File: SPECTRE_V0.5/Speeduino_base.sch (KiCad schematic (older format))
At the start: 213 parts, among them J2 Conn_02x04_Odd_Even, J3 Conn_01x06_Male, Q1 2N7002, Q10 BSP78, Q11 BSP78, Q12 BSP78, Q13 BSP78, Q14 BSP78, Q15 BSP78, Q16 SMD-MOSFET-N-CH-55V-2.1A-AO34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, Q17 AO3401A, Q18 BSP78, Q19 SMD-MOSFET-N-CH-55V-2.1A-AO34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, Q2 CJ2302, Q20 AO3401A, Q21 SMD-MOSFET-N-CH-55V-2.1A-AO34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, Q22 SMD-MOSFET-N-CH-55V-2.1A-AO34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, Q23 AO3401A, Q24 AO3401A, Q25 BSP78, Q26 BSP78, Q3 CJ2302, Q4 CJ2302, Q5 BSP78, Q6 BSP78, Q7 CJ2302, Q8 CJ2302, Q9 CJ2302, U1 MAX9926UAEE+, U2 molex_48pin, U3 LM78M05_TO220, U4 MAX3232, U5 TL431DBZ

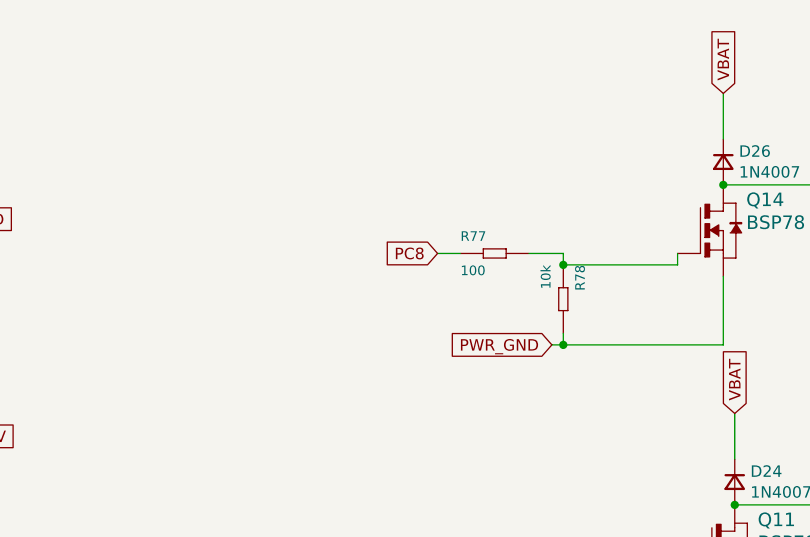
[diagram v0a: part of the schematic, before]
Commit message: boost pin change
update pin def boost pin
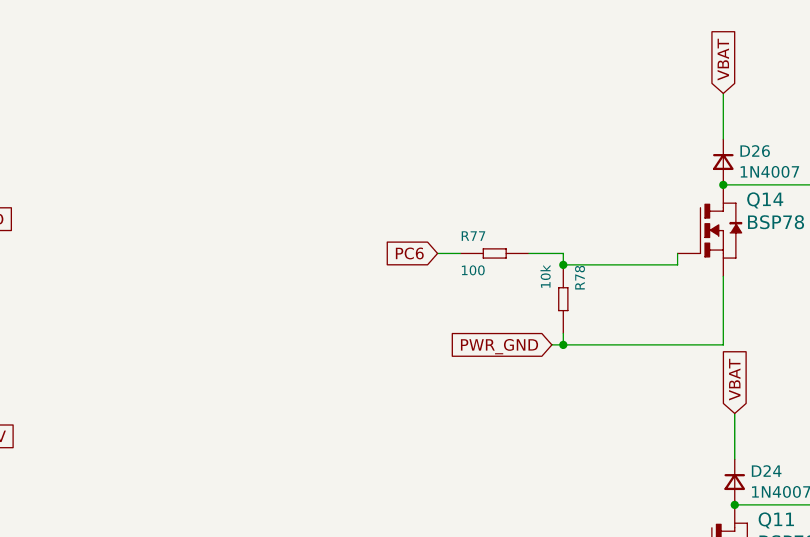
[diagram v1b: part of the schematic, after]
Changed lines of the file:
@@
 PE1
 Text GLabel 14650 1050 0    50   Input ~ 0
-PC8
+PC6
 Text GLabel 14450 3950 0    50   Input ~ 0
 PD3

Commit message: Cleaned and updated the SPECTRE V0.5 Created separate Peak and Hold board.
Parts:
- removed D10: 40V-1A, Speeduino_base:DO-214AC, symbol Speeduino_base-eagle-import:SMD-DIODE-SCHOTTKY-40V-1A(DO-214AC)
- removed D13: Zener 5.1V, Speeduino_base:LED-1206, symbol Speeduino_base-eagle-import:SMD-DIODE-SWITCHING-75V-150MA(D1206)
- added D4: 1N4007, Diode_SMD:D_SMA, symbol Device:D_Small
- added D8: Zener 5.1V, Diode_SMD:D_MiniMELF_Handsoldering, symbol Device:D_Zener_Small
- C27, C28, C29, C30: footprint Capacitor_SMD:C_0603_1608Metric -> Speeduino_base:C0603
- D14: renamed from D22; footprint Speeduino_base:D_SOD-128 -> Diode_SMD:D_SMA
- D20: renamed from D23; footprint Speeduino_base:D_SOD-128 -> Diode_SMD:D_SMA
- D27: renamed from D30; value SS310 -> 1N4007
- D28: renamed from D31; value SS310 -> 1N4007
- D29: renamed from D26; footprint Speeduino_base:D_SOD-128 -> Diode_SMD:D_SMA
- D30: renamed from D24; footprint Speeduino_base:D_SOD-128 -> Diode_SMD:D_SMA
- D31: renamed from D25; footprint Speeduino_base:D_SOD-128 -> Diode_SMD:D_SMA
- D32, D33: value SS310 -> 1N4007
- D6: renamed from D27; value 3.6V -> Zener 3.6V
- Q1: renamed from Q2; value CJ2302 -> AO3400
- Q16: renamed from Q21; value SMD-MOSFET-N-CH-55V-2.1A-AO3422(SOT-23) -> AO3422
- Q17: renamed from Q22; value SMD-MOSFET-N-CH-55V-2.1A-AO3422(SOT-23) -> AO3422
- Q2: renamed from Q1; value 2N7002 -> AO3400
- Q3: renamed from Q4; value CJ2302 -> AO3400
- Q4: renamed from Q7; value CJ2302 -> AO3400
- Q5: renamed from Q9; value CJ2302 -> AO3400
- Q6: renamed from Q8; value CJ2302 -> AO3400
- Q7: renamed from Q3; value CJ2302 -> AO3400
- Q8: renamed from Q19; value SMD-MOSFET-N-CH-55V-2.1A-AO3422(SOT-23) -> AO3422
- Q9: renamed from Q16; value SMD-MOSFET-N-CH-55V-2.1A-AO3422(SOT-23) -> AO3422
- R16: renamed from R76; footprint Resistor_SMD:R_0603_1608Metric_Pad1.05x0.95mm_HandSolder -> Speeduino_base:R0603
- R20: renamed from R72; footprint Resistor_SMD:R_0603_1608Metric_Pad1.05x0.95mm_HandSolder -> Speeduino_base:R0603
- R3: renamed from R2; footprint Resistor_SMD:R_0603_1608Metric_Pad1.05x0.95mm_HandSolder -> Speeduino_base:R0603
- R30: renamed from R98; footprint Resistor_SMD:R_0603_1608Metric_Pad1.05x0.95mm_HandSolder -> Speeduino_base:R0603
- R31: renamed from R99; footprint Resistor_SMD:R_0603_1608Metric_Pad1.05x0.95mm_HandSolder -> Speeduino_base:R0603
- R5: renamed from R75; footprint Resistor_SMD:R_0603_1608Metric_Pad1.05x0.95mm_HandSolder -> Speeduino_base:R0603
- R69: renamed from R84; value 1K -> 1k
- R73: renamed from R85; value 1K -> 1k; footprint Speeduino_base:R_0603_1608Metric_Pad1.05x0.95mm_HandSolder -> Speeduino_base:R0603
- R74: renamed from R80; value 1K -> 1k; footprint Speeduino_base:R_0603_1608Metric_Pad1.05x0.95mm_HandSolder -> Speeduino_base:R0603
- R76: renamed from R87; value 1K8 -> 1k8; footprint Speeduino_base:R_0603_1608Metric_Pad1.05x0.95mm_HandSolder -> Speeduino_base:R0603
- R77: renamed from R82; value 1K8 -> 1k8; footprint Speeduino_base:R_0603_1608Metric_Pad1.05x0.95mm_HandSolder -> Speeduino_base:R0603
- R78: renamed from R86; footprint Speeduino_base:R_0603_1608Metric_Pad1.05x0.95mm_HandSolder -> Speeduino_base:R0603
- R79: renamed from R81; footprint Speeduino_base:R_0603_1608Metric_Pad1.05x0.95mm_HandSolder -> Speeduino_base:R0603
- R80: renamed from R79; footprint Speeduino_base:R_0603_1608Metric_Pad1.05x0.95mm_HandSolder -> Speeduino_base:R0603
- R81: renamed from R88; footprint Speeduino_base:R_0603_1608Metric_Pad1.05x0.95mm_HandSolder -> Speeduino_base:R0603
- R86: renamed from R89; value 1K -> 1k; footprint Speeduino_base:R_0603_1608Metric_Pad1.05x0.95mm_HandSolder -> Speeduino_base:R0603
- R87: renamed from R90; value 1K -> 1k; footprint Speeduino_base:R_0603_1608Metric_Pad1.05x0.95mm_HandSolder -> Speeduino_base:R0603
- R91: renamed from R92; value 1K8 -> 1k8; footprint Speeduino_base:R_0603_1608Metric_Pad1.05x0.95mm_HandSolder -> Speeduino_base:R0603
- R92: renamed from R94; value 1K8 -> 1k8; footprint Speeduino_base:R_0603_1608Metric_Pad1.05x0.95mm_HandSolder -> Speeduino_base:R0603
- R96: renamed from R93; footprint Speeduino_base:R_0603_1608Metric_Pad1.05x0.95mm_HandSolder -> Speeduino_base:R0603
- R97: renamed from R91; footprint Speeduino_base:R_0603_1608Metric_Pad1.05x0.95mm_HandSolder -> Speeduino_base:R0603
- R98: renamed from R95; footprint Speeduino_base:R_0603_1608Metric_Pad1.05x0.95mm_HandSolder -> Speeduino_base:R0603
- R99: renamed from R96; footprint Speeduino_base:R_0603_1608Metric_Pad1.05x0.95mm_HandSolder -> Speeduino_base:R0603
- renumbered C7 to C10, C19 to C11, C8 to C12, C9 to C13, C18 to C14, C10 to C15, C22 to C16, C25 to C17, C26 to C18, C11 to C19, C12 to C20, C13 to C21, C15 to C22, C21 to C23, C20 to C24, C24 to C25, C23 to C26, C14 to C6, C6 to C7, C16 to C8, C17 to C9, D5 to D10, D7 to D11, D8 to D12, D9 to D13, D18 to D15, D11 to D16, D12 to D17, D17 to D18, D15 to D19, D16 to D21, D28 to D22, D29 to D23, D19 to D24, D20 to D25, D21 to D26, D4 to D5, D14 to D7, D6 to D9, J3 to J1, JP13 to JP1, JP16 to JP10, JP17 to JP11, JP3 to JP12, JP5 to JP13, JP11 to JP2, JP12 to JP3, JP14 to JP4, JP10 to JP5, JP9 to JP6, JP2 to JP7, JP4 to JP8, JP1 to JP9, Q20 to Q10, Q17 to Q11, Q15 to Q12, Q18 to Q13, Q5 to Q14, Q6 to Q15, Q10 to Q18, Q14 to Q19, Q11 to Q20, Q23 to Q21, Q24 to Q22, Q12 to Q23, Q13 to Q24, R8 to R10, R6 to R11, R9 to R12, R10 to R13, R11 to R14, R12 to R15, R13 to R17, R74 to R18, R14 to R19, R23 to R2, R16 to R21, R15 to R22, R35 to R23, R17 to R24, R36 to R25, R37 to R26, R18 to R27, R19 to R28, R20 to R29, R21 to R32, R26 to R33, R27 to R34, R22 to R35, R29 to R36, R40 to R37, R24 to R38, R25 to R39, R3 to R4, R41 to R40, R42 to R41, R66 to R42, R28 to R43, R30 to R44, R31 to R45, R67 to R46, R68 to R47, R45 to R48, R32 to R49, R33 to R50, R47 to R51, R50 to R52, R51 to R53, R34 to R56, R56 to R57, R52 to R58, R39 to R59, R5 to R6, R38 to R60, R53 to R61, R57 to R62, R43 to R63, R60 to R64, R44 to R66, R46 to R67, R83 to R68, R4 to R7, R69 to R70, R70 to R71, R71 to R72, R97 to R75, R73 to R8, R48 to R82, R49 to R83, R58 to R84, R77 to R85, R59 to R88, R61 to R89, R7 to R9, R78 to R90, R62 to R93, R63 to R94, R64 to R95, U$2 to U$1, U3 to U2, U5 to U3, U2 to U4, U?1 to U5, U4 to U6
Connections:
- wire segments 569 -> 570
- no-connect marks 52 -> 51
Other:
- moved on the sheet: D6, R31, U3

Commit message: Removed peak&hold driver from this repo. Update resistor values in schematic to values that work. Cleaned up resistor naming.
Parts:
- C27, C28, C29, C30: value 100nF -> 100nf
- R10, R26, R29, R47: value 9.1k -> 9k1
- R25: value 4.7k -> 4K7
- R28, R46, R9: value 4.7k -> 4k7
- R34, R41, R52, R55, R61, R65, R84, R85, R88: value 100 -> 100R
- R44: value 8k3 -> 33k
- R45: value 1k2 -> 5k1
- R66: value 100k -> 10k
- R67: value 1k -> 100R
- R70: value 180 -> 220R
- R71: value 82 -> 100R
- R72: value 560 -> 470R
- R75: value 120 -> 120R
- R78, R79, R96, R97: value 470 -> 470R
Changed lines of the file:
@@
 P 5900 8200
 F 0 "R45" H 5750 8250 42  0000 L BNN
-F 1 "1k2" H 5750 8100 42  0000 L BNN
+F 1 "5k1" H 5750 8100 42  0000 L BNN
 F 2 "Speeduino_base:R0603" H 5900 8200 50  0001 C CNN
 F 3 "" H 5900 8200 50  0001 C CNN
@@
 P 9650 10000
 F 0 "R65" H 9500 10050 42  0000 L BNN
-F 1 "100" H 9500 9900 42  0000 L BNN
+F 1 "100R" H 9500 9900 42  0000 L BNN
 F 2 "Speeduino_base:R0603" H 9650 10000 50  0001 C CNN
 F 3 "" H 9650 10000 50  0001 C CNN
@@
 P 14700 3950
 F 0 "R84" H 14550 4000 42  0000 L BNN
-F 1 "100" H 14550 3850 42  0000 L BNN
+F 1 "100R" H 14550 3850 42  0000 L BNN
 F 2 "Speeduino_base:R0603" H 14700 3950 50  0001 C CNN
 F 3 "" H 14700 3950 50  0001 C CNN
@@
 P 7650 3200
 F 0 "R55" H 7500 3250 42  0000 L BNN
-F 1 "100" H 7500 3100 42  0000 L BNN
+F 1 "100R" H 7500 3100 42  0000 L BNN
 F 2 "Speeduino_base:R0603" H 7650 3200 50  0001 C CNN
 F 3 "" H 7650 3200 50  0001 C CNN
@@
 P 4350 3700
 F 0 "R34" H 4200 3750 42  0000 L BNN
-F 1 "100" H 4200 3600 42  0000 L BNN
+F 1 "100R" H 4200 3600 42  0000 L BNN
 F 2 "Speeduino_base:R0603" H 4350 3700 50  0001 C CNN
 F 3 "" H 4350 3700 50  0001 C CNN
@@
 P 8350 10000
 F 0 "R61" H 8200 10050 42  0000 L BNN
-F 1 "100" H 8200 9900 42  0000 L BNN
+F 1 "100R" H 8200 9900 42  0000 L BNN
 F 2 "Speeduino_base:R0603" H 8350 10000 50  0001 C CNN
 F 3 "" H 8350 10000 50  0001 C CNN
@@
 P 6950 10000
 F 0 "R52" H 6800 10050 42  0000 L BNN
-F 1 "100" H 6800 9900 42  0000 L BNN
+F 1 "100R" H 6800 9900 42  0000 L BNN
 F 2 "Speeduino_base:R0603" H 6950 10000 50  0001 C CNN
 F 3 "" H 6950 10000 50  0001 C CNN
@@
 P 5450 10000
 F 0 "R41" H 5300 10050 42  0000 L BNN
-F 1 "100" H 5300 9900 42  0000 L BNN
+F 1 "100R" H 5300 9900 42  0000 L BNN
 F 2 "Speeduino_base:R0603" H 5450 10000 50  0001 C CNN
 F 3 "" H 5450 10000 50  0001 C CNN
@@
 P 14950 2450
 F 0 "R88" H 14800 2500 42  0000 L BNN
-F 1 "100" H 14800 2350 42  0000 L BNN
+F 1 "100R" H 14800 2350 42  0000 L BNN
 F 2 "Speeduino_base:R0603" H 14950 2450 50  0001 C CNN
 F 3 "" H 14950 2450 50  0001 C CNN
@@
 P 10050 7950
 F 0 "R67" H 9900 8000 42  0000 L BNN
-F 1 "1k" H 9900 7850 42  0000 L BNN
+F 1 "100R" H 9900 7850 42  0000 L BNN
 F 2 "Speeduino_base:R0603" H 10050 7950 50  0001 C CNN
 F 3 "" H 10050 7950 50  0001 C CNN
@@
 P 9750 8150
 F 0 "R66" H 9600 8200 42  0000 L BNN
-F 1 "100k" H 9600 8050 42  0000 L BNN
+F 1 "10k" H 9600 8050 42  0000 L BNN
 F 2 "Speeduino_base:R0603" H 9750 8150 50  0001 C CNN
 F 3 "" H 9750 8150 50  0001 C CNN
@@
 P 3150 8950
 F 0 "R25" H 3000 9009 59  0000 L BNN
-F 1 "4.7k" H 3000 8820 59  0000 L BNN
+F 1 "4K7" H 3000 8820 59  0000 L BNN
 F 2 "Speeduino_base:R0603" H 3150 8950 50  0001 C CNN
 F 3 "" H 3150 8950 50  0001 C CNN
@@
 P 3150 9550
 F 0 "R26" H 3000 9609 59  0000 L BNN
-F 1 "9.1k" H 3000 9420 59  0000 L BNN
+F 1 "9k1" H 3000 9420 59  0000 L BNN
 F 2 "Speeduino_base:R0603" H 3150 9550 50  0001 C CNN
 F 3 "" H 3150 9550 50  0001 C CNN
@@
 P 3300 7150
 F 0 "R28" H 3150 7209 59  0000 L BNN
-F 1 "4.7k" H 3150 7020 59  0000 L BNN
+F 1 "4k7" H 3150 7020 59  0000 L BNN
 F 2 "Speeduino_base:R0603" H 3300 7150 50  0001 C CNN
 F 3 "" H 3300 7150 50  0001 C CNN
@@
 P 3300 7750
 F 0 "R29" H 3150 7809 59  0000 L BNN
-F 1 "9.1k" H 3150 7620 59  0000 L BNN
+F 1 "9k1" H 3150 7620 59  0000 L BNN
 F 2 "Speeduino_base:R0603" H 3300 7750 50  0001 C CNN
 F 3 "" H 3300 7750 50  0001 C CNN
@@
 P 1350 7100
 F 0 "R9" H 1200 7159 59  0000 L BNN
-F 1 "4.7k" H 1200 6970 59  0000 L BNN
+F 1 "4k7" H 1200 6970 59  0000 L BNN
 F 2 "Speeduino_base:R0603" H 1350 7100 50  0001 C CNN
 F 3 "" H 1350 7100 50  0001 C CNN
@@
 P 1350 7700
 F 0 "R10" H 1200 7759 59  0000 L BNN
-F 1 "9.1k" H 1200 7570 59  0000 L BNN
+F 1 "9k1" H 1200 7570 59  0000 L BNN
 F 2 "Speeduino_base:R0603" H 1350 7700 50  0001 C CNN
 F 3 "" H 1350 7700 50  0001 C CNN
@@
 P 5950 4650
 F 0 "R46" H 5800 4709 59  0000 L BNN
-F 1 "4.7k" H 5800 4520 59  0000 L BNN
+F 1 "4k7" H 5800 4520 59  0000 L BNN
 F 2 "Speeduino_base:R0603" H 5950 4650 50  0001 C CNN
 F 3 "" H 5950 4650 50  0001 C CNN
@@
 P 5950 5250
 F 0 "R47" H 5800 5309 59  0000 L BNN
-F 1 "9.1k" H 5800 5120 59  0000 L BNN
+F 1 "9k1" H 5800 5120 59  0000 L BNN
 F 2 "Speeduino_base:R0603" H 5950 5250 50  0001 C CNN
 F 3 "" H 5950 5250 50  0001 C CNN
@@
 P 11350 1300
 F 0 "R72" H 11200 1350 42  0000 L BNN
-F 1 "560" H 11200 1200 42  0000 L BNN
+F 1 "470R" H 11200 1200 42  0000 L BNN
 F 2 "Speeduino_base:R0603" H 11350 1300 50  0001 C CNN
 F 3 "" H 11350 1300 50  0001 C CNN
@@
 P 11350 900
 F 0 "R71" H 11200 950 42  0000 L BNN
-F 1 "82" H 11200 800 42  0000 L BNN
+F 1 "100R" H 11200 800 42  0000 L BNN
 F 2 "Speeduino_base:R0603" H 11350 900 50  0001 C CNN
 F 3 "" H 11350 900 50  0001 C CNN
@@
 P 11350 500
 F 0 "R70" H 11200 550 42  0000 L BNN
-F 1 "180" H 11200 400 42  0000 L BNN
+F 1 "220R" H 11200 400 42  0000 L BNN
 F 2 "Speeduino_base:R0603" H 11350 500 50  0001 C CNN
 F 3 "" H 11350 500 50  0001 C CNN
@@
 P 5900 7700
 F 0 "R44" H 5750 7750 42  0000 L BNN
-F 1 "8k3" H 5750 7600 42  0000 L BNN
+F 1 "33k" H 5750 7600 42  0000 L BNN
 F 2 "Speeduino_base:R0603" H 5900 7700 50  0001 C CNN
 F 3 "" H 5900 7700 50  0001 C CNN
@@
 P 14900 1050
 F 0 "R85" H 14750 1100 42  0000 L BNN
-F 1 "100" H 14750 950 42  0000 L BNN
+F 1 "100R" H 14750 950 42  0000 L BNN
 F 2 "Speeduino_base:R0603" H 14900 1050 50  0001 C CNN
 F 3 "" H 14900 1050 50  0001 C CNN
@@
 P 15400 4850
 F 0 "C29" V 15171 4850 50  0000 C CNN
-F 1 "100nF" V 15262 4850 50  0000 C CNN
+F 1 "100nf" V 15262 4850 50  0000 C CNN
 F 2 "Speeduino_base:C0603" H 15400 4850 50  0001 C CNN
 F 3 "~" H 15400 4850 50  0001 C CNN
@@
 P 15050 6750
 F 0 "C28" H 15142 6796 50  0000 L CNN
-F 1 "100nF" H 15142 6705 50  0000 L CNN
+F 1 "100nf" H 15142 6705 50  0000 L CNN
 F 2 "Speeduino_base:C0603" H 15050 6750 50  0001 C CNN
 F 3 "~" H 15050 6750 50  0001 C CNN
@@
 P 15450 6900
 F 0 "C30" V 15221 6900 50  0000 C CNN
-F 1 "100nF" V 15312 6900 50  0000 C CNN
+F 1 "100nf" V 15312 6900 50  0000 C CNN
 F 2 "Speeduino_base:C0603" H 15450 6900 50  0001 C CNN
 F 3 "~" H 15450 6900 50  0001 C CNN
@@
 P 14750 6750
 F 0 "C27" H 14842 6796 50  0000 L CNN
-F 1 "100nF" H 14842 6705 50  0000 L CNN
+F 1 "100nf" H 14842 6705 50  0000 L CNN
 F 2 "Speeduino_base:C0603" H 14750 6750 50  0001 C CNN
 F 3 "~" H 14750 6750 50  0001 C CNN
@@
 P 12450 6250
 F 0 "R75" H 12300 6300 42  0000 L BNN
-F 1 "120" H 12300 6150 42  0000 L BNN
+F 1 "120R" H 12300 6150 42  0000 L BNN
 F 2 "Speeduino_base:R0603" H 12450 6250 50  0001 C CNN
 F 3 "" H 12450 6250 50  0001 C CNN
@@
 P 15650 10850
 F 0 "R96" H 15709 10896 50  0000 L CNN
-F 1 "470" H 15709 10805 50  0000 L CNN
+F 1 "470R" H 15709 10805 50  0000 L CNN
 F 2 "Speeduino_base:R0603" H 15650 10850 50  0001 C CNN
 F 3 "~" H 15650 10850 50  0001 C CNN
@@
 P 15800 9650
 F 0 "R97" H 15859 9696 50  0000 L CNN
-F 1 "470" H 15859 9605 50  0000 L CNN
+F 1 "470R" H 15859 9605 50  0000 L CNN
 F 2 "Speeduino_base:R0603" H 15800 9650 50  0001 C CNN
 F 3 "~" H 15800 9650 50  0001 C CNN
@@
 P 13050 10850
 F 0 "R79" H 13109 10896 50  0000 L CNN
-F 1 "470" H 13109 10805 50  0000 L CNN
+F 1 "470R" H 13109 10805 50  0000 L CNN
 F 2 "Speeduino_base:R0603" H 13050 10850 50  0001 C CNN
 F 3 "~" H 13050 10850 50  0001 C CNN
@@
 P 13050 9650
 F 0 "R78" H 13109 9696 50  0000 L CNN
-F 1 "470" H 13109 9605 50  0000 L CNN
+F 1 "470R" H 13109 9605 50  0000 L CNN
 F 2 "Speeduino_base:R0603" H 13050 9650 50  0001 C CNN
 F 3 "~" H 13050 9650 50  0001 C CNN
